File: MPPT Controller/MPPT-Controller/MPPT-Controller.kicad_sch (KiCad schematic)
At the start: 50 parts, among them J1 Conn_01x02_Pin, J2 Conn_01x02_Pin, J3 Conn_01x02_Pin, J4 Conn_01x02_Pin, J6 Conn_01x02_Pin, Q1 IRL540N, SW1 SW_SPDT, U1 ADS1115IDGS, U4 LM1117DT-3.3, U5 LM2596S-ADJ, U6 TC4422, U7 ADS1115IDGS

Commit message: Compact
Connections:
- net GND: now also R1.2; no longer R1.1
- net at C13.1, R21.1, R22.1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: now also R1.1; no longer R1.2
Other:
- moved on the sheet: D7, R1
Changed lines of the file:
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@@
 	(symbol
 		(lib_id "Device:R")
-		(at 160.02 31.75 90)
+		(at 160.02 31.75 270)
+		(mirror x)
 		(unit 1)
 		(exclude_from_sim no)
@@
 		(dnp no)
 		(property "Reference" "R1"
-			(at 161.544 34.036 90)
+			(at 158.496 34.036 90)
 			(effects
 				(font
@@
 		)
 		(property "Value" "1k"
-			(at 161.544 31.75 90)
+			(at 158.496 31.75 90)
 			(effects
 				(font
@@
 	(symbol
 		(lib_id "ScottoKeebs:Placeholder_Diode")
-		(at 179.07 54.61 270)
+		(at 179.07 54.61 90)
+		(mirror x)
 		(unit 1)
 		(exclude_from_sim no)
@@
 		(dnp no)
 		(property "Reference" "D7"
-			(at 177.165 55.245 90)
+			(at 180.975 55.245 90)
 			(effects
 				(font
@@
 		)
 		(property "Value" "Diode"
-			(at 177.165 52.705 90)
-			(effects
-				(font
+			(at 180.975 52.705 90)
+			(effects
+				(font

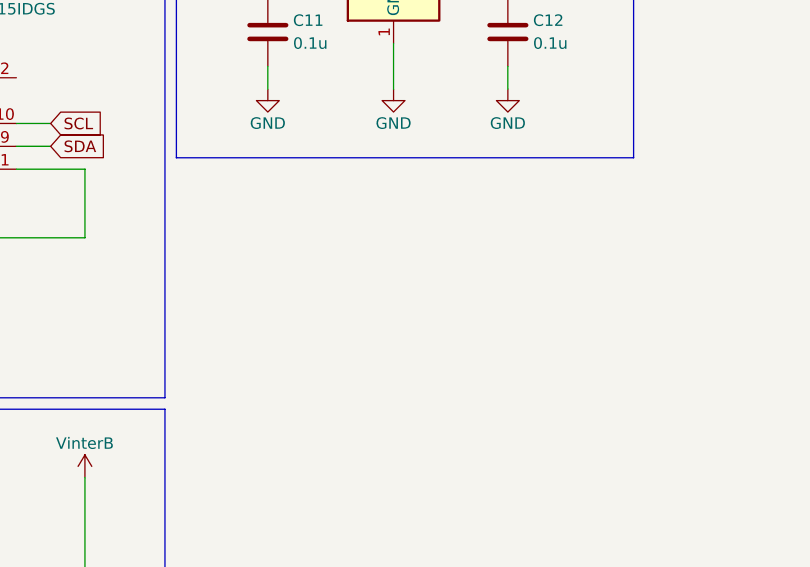
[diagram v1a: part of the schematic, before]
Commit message: Add Heatink
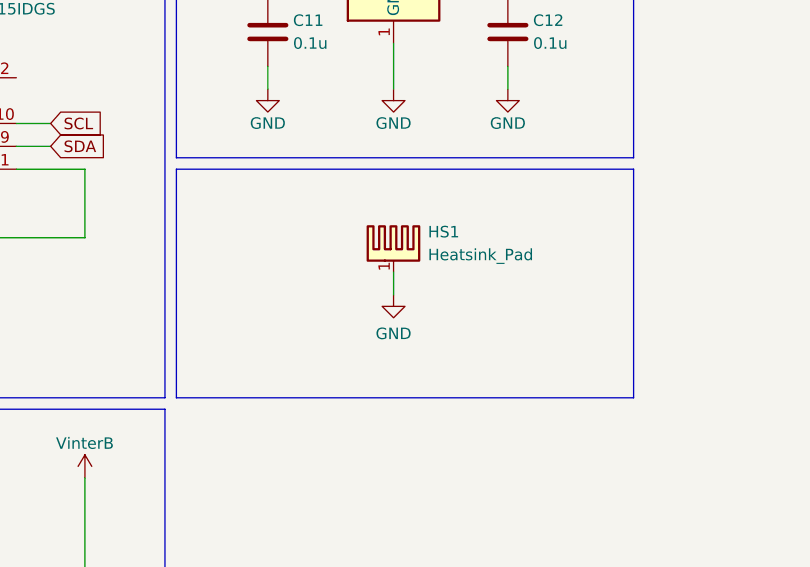
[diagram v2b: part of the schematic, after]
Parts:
- added HS1: Heatsink_Pad, Heatsink:Heatsink_35x26mm_1xFixation3mm_Fischer-SK486-35, symbol Mechanical:Heatsink_Pad
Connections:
- net GND: now also HS1.1
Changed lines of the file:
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@@
 	)
 	(rectangle
+		(start 171.45 104.14)
+		(end 222.25 129.54)
+		(stroke
+			(width 0)
+			(type default)
+		)
+		(fill
+			(type none)
+		)
+	)
+	(rectangle
 		(start 13.97 72.39)
 		(end 64.77 196.85)
@@
 	(wire
 		(pts
+			(xy 195.58 115.57) (xy 195.58 118.11)
+		)
+		(stroke
+			(width 0)
+			(type default)
+		)
+	)
+	(wire
+		(pts
 			(xy 181.61 92.71) (xy 181.61 95.25)
 		)
@@
 	)
 	(symbol
+		(lib_id "power:GND")
+		(at 195.58 118.11 0)
+		(unit 1)
+		(exclude_from_sim no)
+		(in_bom yes)
+		(on_board yes)
+		(dnp no)
+		(property "Reference" "#PWR059"
+			(at 195.58 124.46 0)
+			(effects
+				(font
+					(size 1.27 1.27)
+				)
+				(hide yes)
+			)
+		)
+		(property "Value" "GND"
+			(at 195.58 122.428 0)
+			(effects
+				(font
+					(size 1.27 1.27)
+				)
+			)
+		)
+		(property "Footprint" ""
+			(at 195.58 118.11 0)
+			(effects
+				(font
+					(size 1.27 1.27)
+				)
+				(hide yes)
+			)
+		)
+		(property "Datasheet" ""
+			(at 195.58 118.11 0)
+			(effects
+				(font
+					(size 1.27 1.27)
+				)
+				(hide yes)
+			)
+		)
+		(property "Description" "Power symbol creates a global label with name \"GND\" , ground"
+			(at 195.58 118.11 0)
+			(effects
+				(font
+					(size 1.27 1.27)
+				)
+				(hide yes)
+			)
+		)
+		(pin "1"
+		)
+		(instances
+			(project "MPPT-Controller"
+				(path "/3478fe58-6c48-40fd-90f3-a0feb3af5722"
+					(reference "#PWR059")
+					(unit 1)
+				)
+			)
+		)
+	)
+	(symbol
 		(lib_id "Device:R")
 		(at 31.75 45.72 0)
@@
 					(unit 1)
 				)
+			)
+		)
+	)
+	(symbol
+		(lib_id "Mechanical:Heatsink_Pad")
+		(at 195.58 113.03 0)
+		(unit 1)
+		(exclude_from_sim no)
+		(in_bom yes)
+		(on_board yes)
+		(dnp no)
+		(fields_autoplaced yes)
+		(property "Reference" "HS1"
+			(at 199.39 111.1249 0)
+			(effects
+				(font
+					(size 1.27 1.27)
+				)
+				(justify left)
+			)
+		)
+		(property "Value" "Heatsink_Pad"
+			(at 199.39 113.6649 0)
+			(effects
+				(font
+					(size 1.27 1.27)
+				)
+				(justify left)
+			)
+		)
+		(property "Footprint" "Heatsink:Heatsink_35x26mm_1xFixation3mm_Fischer-SK486-35"
+			(at 195.8848 114.3 0)
+			(effects
+				(font
+					(size 1.27 1.27)
+				)
+				(hide yes)
+			)
+		)
+		(property "Datasheet" "~"
+			(at 195.8848 114.3 0)
+			(effects
+				(font
+					(size 1.27 1.27)
+				)
+				(hide yes)
+			)
+		)
+		(property "Description" "Heatsink with electrical connection, 1 pin"
+			(at 195.58 113.03 0)
+			(effects
+				(font
+					(size 1.27 1.27)
+				)
+				(hide yes)
+			)
+		)
+		(pin "1"
+		)
+		(instances
+			(project "MPPT-Controller"
+				(path "/3478fe58-6c48-40fd-90f3-a0feb3af5722"
+					(reference "HS1")
+					(unit 1)
+				)

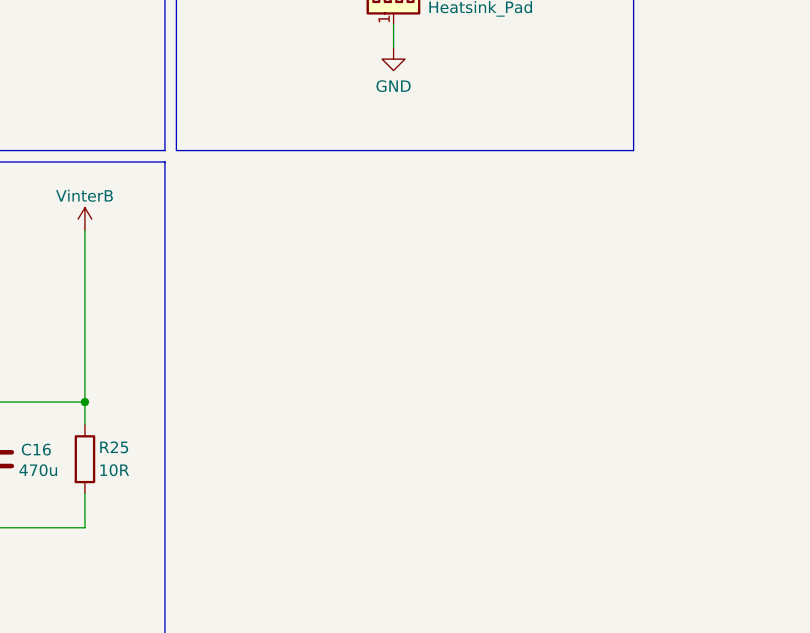
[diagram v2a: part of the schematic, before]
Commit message: Add Fan Connector
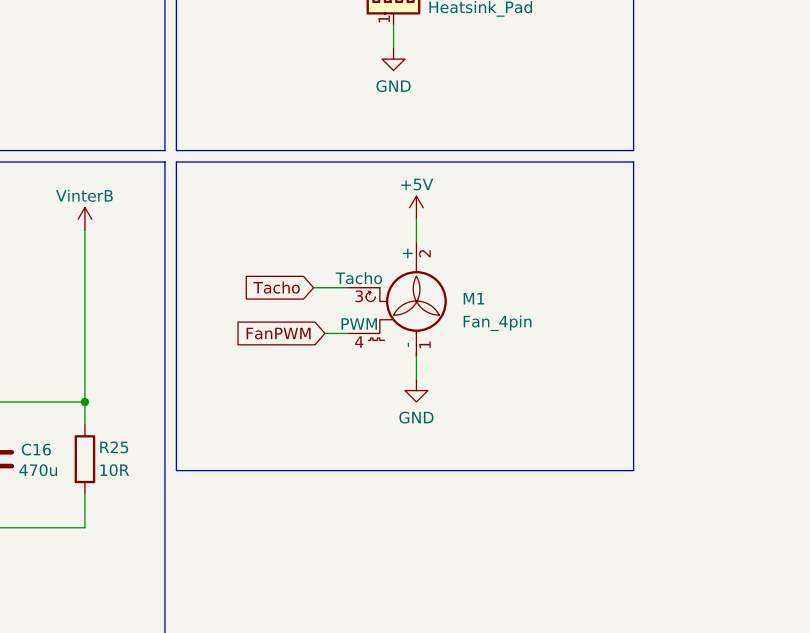
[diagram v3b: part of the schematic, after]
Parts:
- added M1: Fan_4pin, Connector:FanPinHeader_1x04_P2.54mm_Vertical, symbol Motor:Fan_4pin
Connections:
- net +5V: now also M1.2 (+)
- net GND: now also M1.1 (-)
- new net FanPWM: M1.4 (PWM)
- new net Tacho: M1.3 (Tacho)

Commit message: Layout
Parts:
- HS1: footprint Heatsink:Heatsink_35x26mm_1xFixation3mm_Fischer-SK486-35 -> Heatsink:Heatsink_AAVID_576802B03900G
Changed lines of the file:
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@@
 			)
 		)
-		(property "Footprint" "Heatsink:Heatsink_35x26mm_1xFixation3mm_Fischer-SK486-35"
+		(property "Footprint" "Heatsink:Heatsink_AAVID_576802B03900G"
 			(at 195.8848 114.3 0)
 			(effects

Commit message: Layout
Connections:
- net GND: no longer HS1.1
- net VinterA: now also HS1.1
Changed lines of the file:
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@@
 	)
 	(symbol
-		(lib_id "power:GND")
-		(at 195.58 118.11 0)
-		(unit 1)
-		(exclude_from_sim no)
-		(in_bom yes)
-		(on_board yes)
-		(dnp no)
-		(property "Reference" "#PWR059"
-			(at 195.58 124.46 0)
-			(effects
-				(font
-					(size 1.27 1.27)
-				)
-				(hide yes)
-			)
-		)
-		(property "Value" "GND"
-			(at 195.58 122.428 0)
-			(effects
-				(font
-					(size 1.27 1.27)
-				)
-			)
-		)
-		(property "Footprint" ""
-			(at 195.58 118.11 0)
-			(effects
-				(font
-					(size 1.27 1.27)
-				)
-				(hide yes)
-			)
-		)
-		(property "Datasheet" ""
-			(at 195.58 118.11 0)
-			(effects
-				(font
-					(size 1.27 1.27)
-				)
-				(hide yes)
-			)
-		)
-		(property "Description" "Power symbol creates a global label with name \"GND\" , ground"
-			(at 195.58 118.11 0)
-			(effects
-				(font
-					(size 1.27 1.27)
-				)
-				(hide yes)
-			)
-		)
-		(pin "1"
-		)
-		(instances
-			(project "MPPT-Controller"
-				(path "/3478fe58-6c48-40fd-90f3-a0feb3af5722"
-					(reference "#PWR059")
-					(unit 1)
-				)
-			)
-		)
-	)
-	(symbol
 		(lib_id "Device:R")
 		(at 31.75 45.72 0)
@@
 					(unit 1)
 				)
+			)
+		)
+	)
+	(symbol
+		(lib_id "power:VAA")
+		(at 195.58 118.11 180)
+		(unit 1)
+		(exclude_from_sim no)
+		(in_bom yes)
+		(on_board yes)
+		(dnp no)
+		(property "Reference" "#PWR059"
+			(at 195.58 114.3 0)
+			(effects
+				(font
+					(size 1.27 1.27)
+				)
+				(hide yes)
+			)
+		)
+		(property "Value" "VinterA"
+			(at 195.58 121.92 0)
+			(effects
+				(font
+					(size 1.27 1.27)
+				)
+			)
+		)
+		(property "Footprint" ""
+			(at 195.58 118.11 0)
+			(effects
+				(font
+					(size 1.27 1.27)
+				)
+				(hide yes)
+			)
+		)
+		(property "Datasheet" ""
+			(at 195.58 118.11 0)
+			(effects
+				(font
+					(size 1.27 1.27)
+				)
+				(hide yes)
+			)
+		)
+		(property "Description" "Power symbol creates a global label with name \"VAA\""
+			(at 195.58 118.11 0)
+			(effects
+				(font
+					(size 1.27 1.27)
+				)
+				(hide yes)
+			)
+		)
+		(pin "1"
+		)
+		(instances
+			(project "MPPT-Controller"
+				(path "/3478fe58-6c48-40fd-90f3-a0feb3af5722"
+					(reference "#PWR059")
+					(unit 1)
+				)

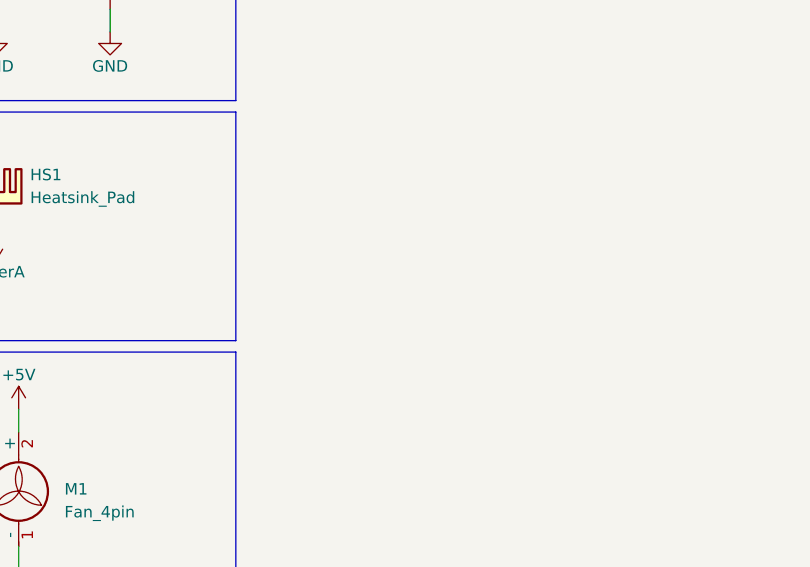
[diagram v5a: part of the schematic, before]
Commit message: Add thermistor
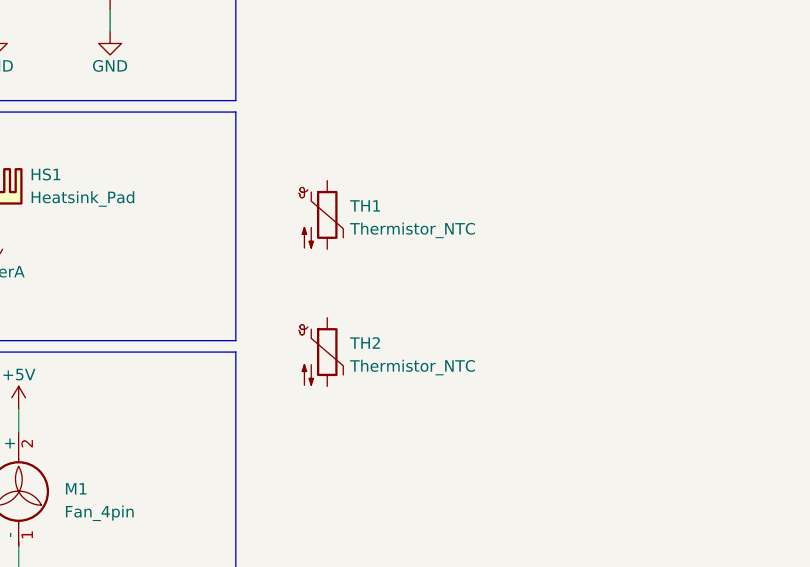
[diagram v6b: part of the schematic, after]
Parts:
- added TH1, TH2: Thermistor_NTC, Resistor_THT:R_Axial_DIN0204_L3.6mm_D1.6mm_P1.90mm_Vertical, symbol Device:Thermistor_NTC
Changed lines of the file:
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@@
 	)
 	(symbol
+		(lib_id "Device:Thermistor_NTC")
+		(at 232.41 130.81 0)
+		(unit 1)
+		(exclude_from_sim no)
+		(in_bom yes)
+		(on_board yes)
+		(dnp no)
+		(fields_autoplaced yes)
+		(property "Reference" "TH2"
+			(at 234.95 129.8574 0)
+			(effects
+				(font
+					(size 1.27 1.27)
+				)
+				(justify left)
+			)
+		)
+		(property "Value" "Thermistor_NTC"
+			(at 234.95 132.3974 0)
+			(effects
+				(font
+					(size 1.27 1.27)
+				)
+				(justify left)
+			)
+		)
+		(property "Footprint" "Resistor_THT:R_Axial_DIN0204_L3.6mm_D1.6mm_P1.90mm_Vertical"
+			(at 232.41 129.54 0)
+			(effects
+				(font
+					(size 1.27 1.27)
+				)
+				(hide yes)
+			)
+		)
+		(property "Datasheet" "~"
+			(at 232.41 129.54 0)
+			(effects
+				(font
+					(size 1.27 1.27)
+				)
+				(hide yes)
+			)
+		)
+		(property "Description" "Temperature dependent resistor, negative temperature coefficient"
+			(at 232.41 130.81 0)
+			(effects
+				(font
+					(size 1.27 1.27)
+				)
+				(hide yes)
+			)
+		)
+		(pin "2"
+		)
+		(pin "1"
+		)
+		(instances
+			(project "MPPT-Controller"
+				(path "/3478fe58-6c48-40fd-90f3-a0feb3af5722"
+					(reference "TH2")
+					(unit 1)
+				)
+			)
+		)
+	)
+	(symbol
 		(lib_id "Device:R")
 		(at 46.99 31.75 90)
@@
 					(unit 1)
 				)
+			)
+		)
+	)
+	(symbol
+		(lib_id "Device:Thermistor_NTC")
+		(at 232.41 115.57 0)
+		(unit 1)
+		(exclude_from_sim no)
+		(in_bom yes)
+		(on_board yes)
+		(dnp no)
+		(fields_autoplaced yes)
+		(property "Reference" "TH1"
+			(at 234.95 114.6174 0)
+			(effects
+				(font
+					(size 1.27 1.27)
+				)
+				(justify left)
+			)
+		)
+		(property "Value" "Thermistor_NTC"
+			(at 234.95 117.1574 0)
+			(effects
+				(font
+					(size 1.27 1.27)
+				)
+				(justify left)
+			)
+		)
+		(property "Footprint" "Resistor_THT:R_Axial_DIN0204_L3.6mm_D1.6mm_P1.90mm_Vertical"
+			(at 232.41 114.3 0)
+			(effects
+				(font
+					(size 1.27 1.27)
+				)
+				(hide yes)
+			)
+		)
+		(property "Datasheet" "~"
+			(at 232.41 114.3 0)
+			(effects
+				(font
+					(size 1.27 1.27)
+				)
+				(hide yes)
+			)
+		)
+		(property "Description" "Temperature dependent resistor, negative temperature coefficient"
+			(at 232.41 115.57 0)
+			(effects
+				(font
+					(size 1.27 1.27)
+				)
+				(hide yes)
+			)
+		)
+		(pin "2"
+		)
+		(pin "1"
+		)
+		(instances
+			(project ""
+				(path "/3478fe58-6c48-40fd-90f3-a0feb3af5722"
+					(reference "TH1")
+					(unit 1)
+				)

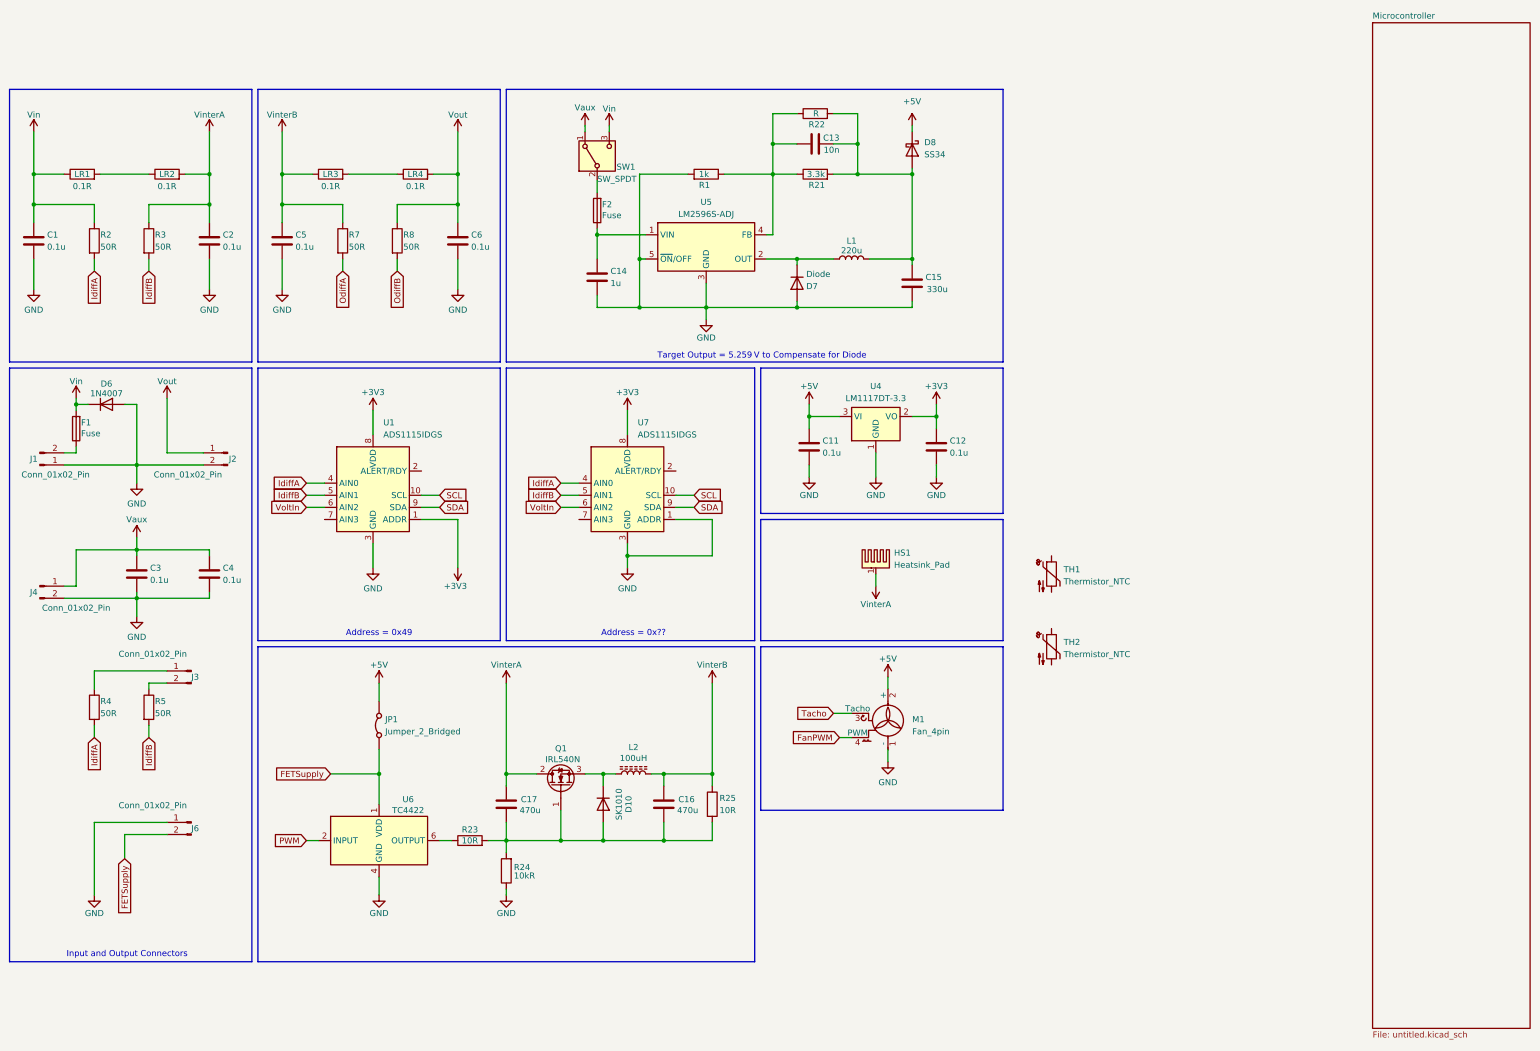
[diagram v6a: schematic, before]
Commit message: Add ADC Channels
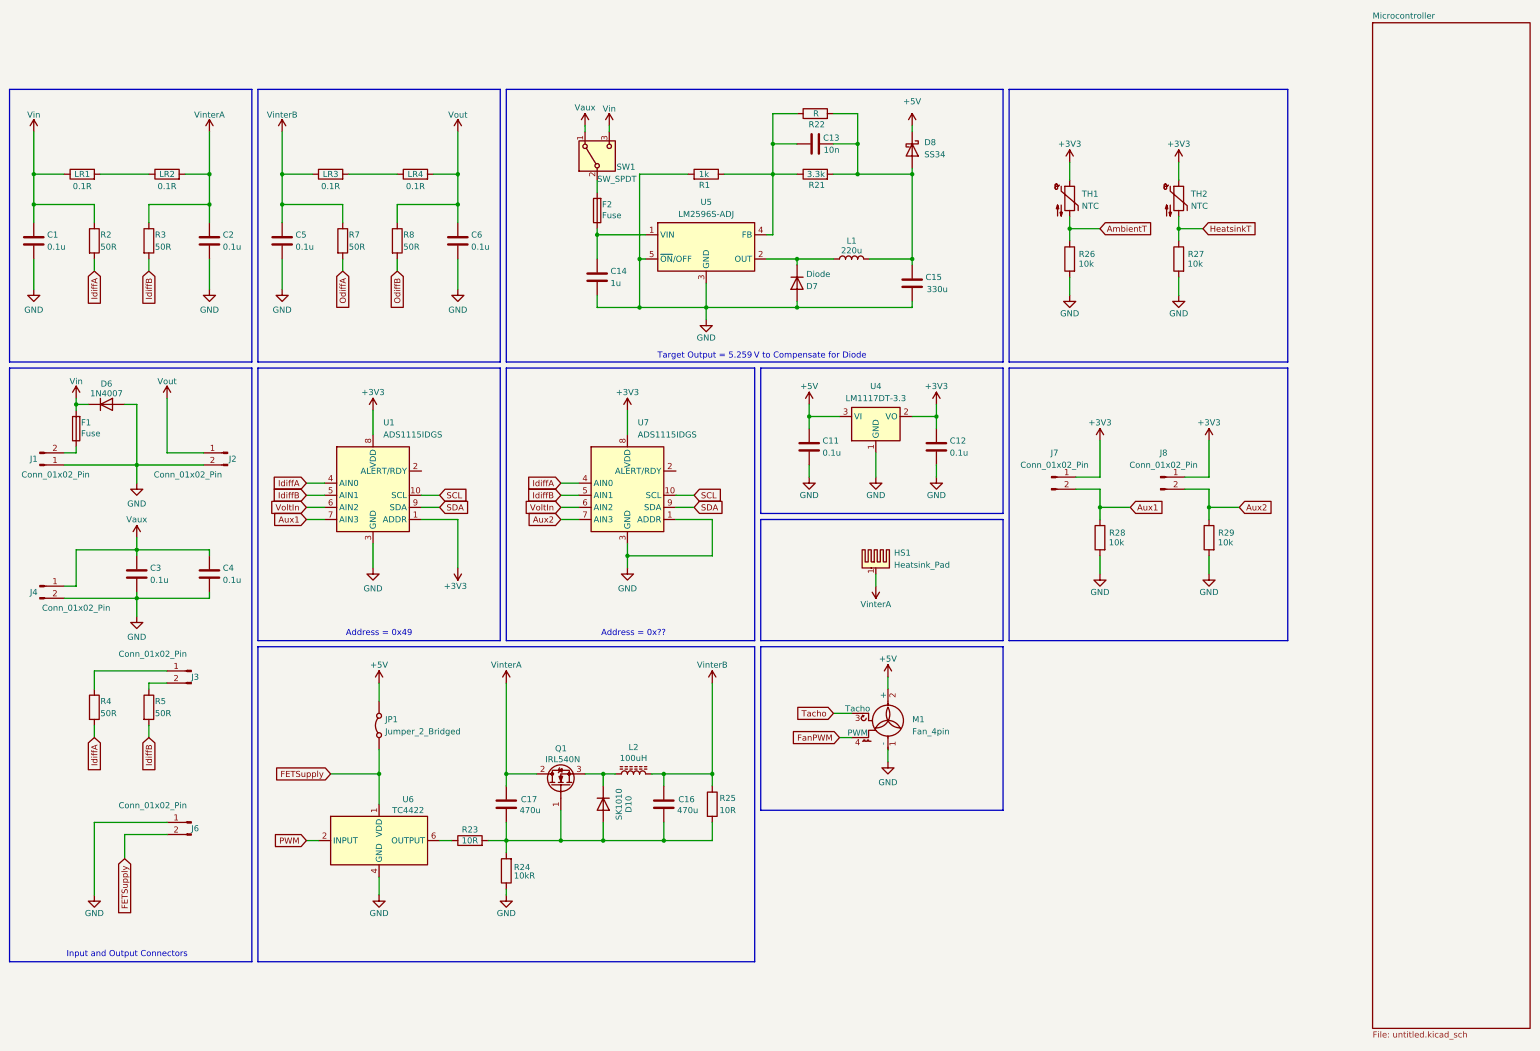
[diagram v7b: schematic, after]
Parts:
- added J7, J8: Conn_01x02_Pin, Connector_PinHeader_2.54mm:PinHeader_1x02_P2.54mm_Vertical, symbol Connector:Conn_01x02_Pin
- added R26, R27, R28, R29: 10k, LED_SMD:LED_0805_2012Metric_Pad1.15x1.40mm_HandSolder, symbol Device:R
- TH1, TH2: value Thermistor_NTC -> NTC
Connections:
- net +3V3: now also TH1.1, TH2.1, J7.1 (Pin_1), J8.1 (Pin_1)
- net GND: now also R26.2, R27.2, R28.2, R29.2
- net Aux2: now reaches U7.7 (AIN3)
- net Aux2: now also J8.2 (Pin_2), R29.1
- net HeatsinkT: now reaches TH2.2
- net HeatsinkT: now also R27.1
- net Aux1: now reaches U1.7 (AIN3)
- net Aux1: now also J7.2 (Pin_2), R28.1
- net AmbientT: now reaches TH1.2
- net AmbientT: now also R26.1
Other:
- moved on the sheet: TH1, TH2
